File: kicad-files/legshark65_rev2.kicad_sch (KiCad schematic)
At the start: 183 parts, among them J1 ARM JTAG, J2 Conn_01x04, SW1 K2-1187SQ-A4SW-06, SW2 PCM12SMTR, T2 53261-0471, U1 STM32F411CEU6, U3 AT24C256C-SSHL-T, Y1 TAXM8M4RFDCET2T

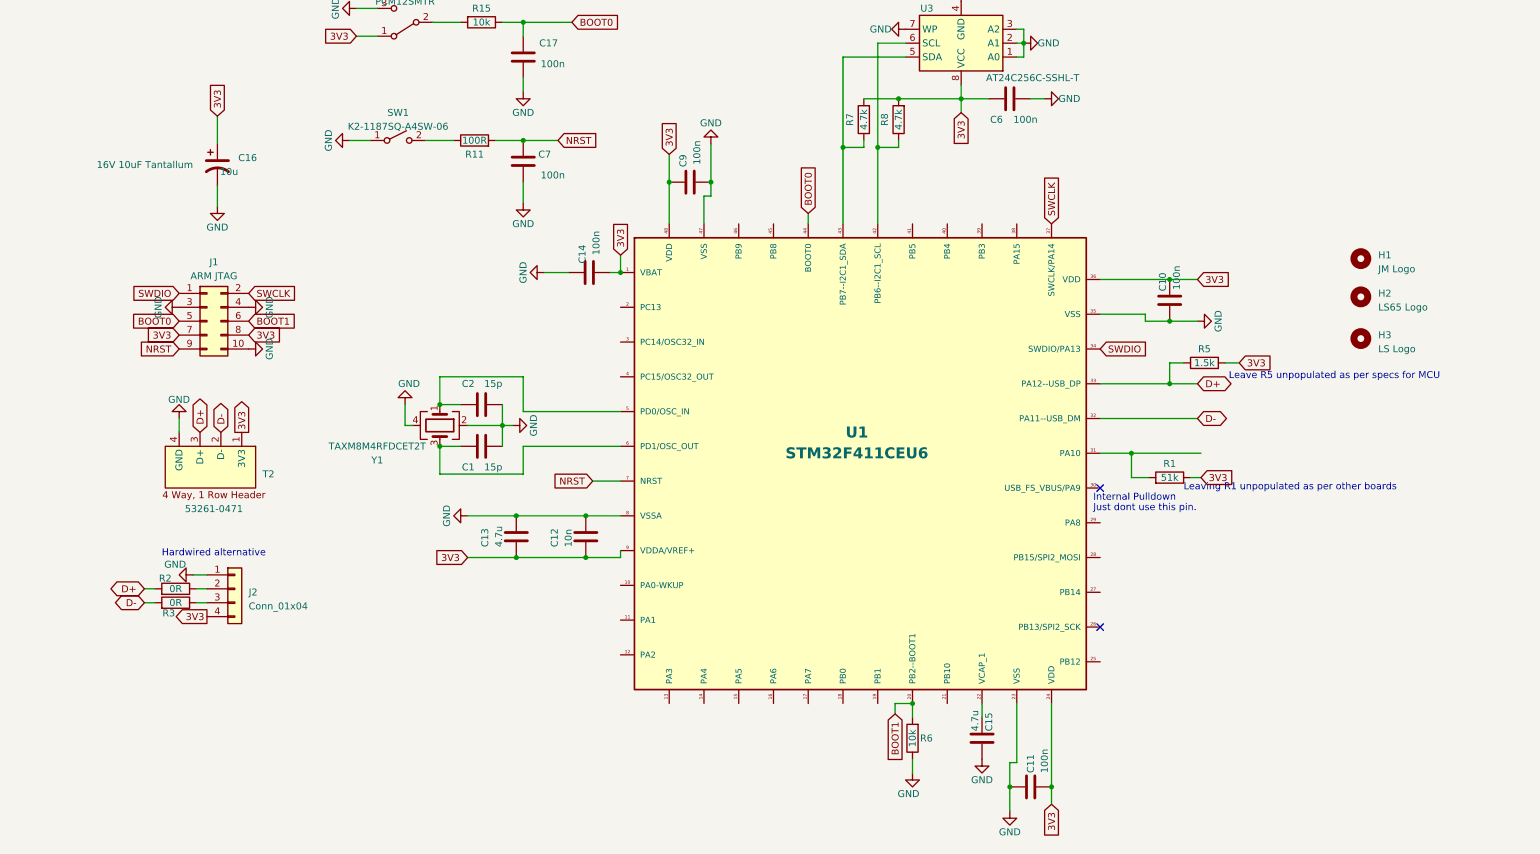
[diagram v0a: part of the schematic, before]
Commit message: Added the 5V to 3V3 stepdown schematic from db to the mb
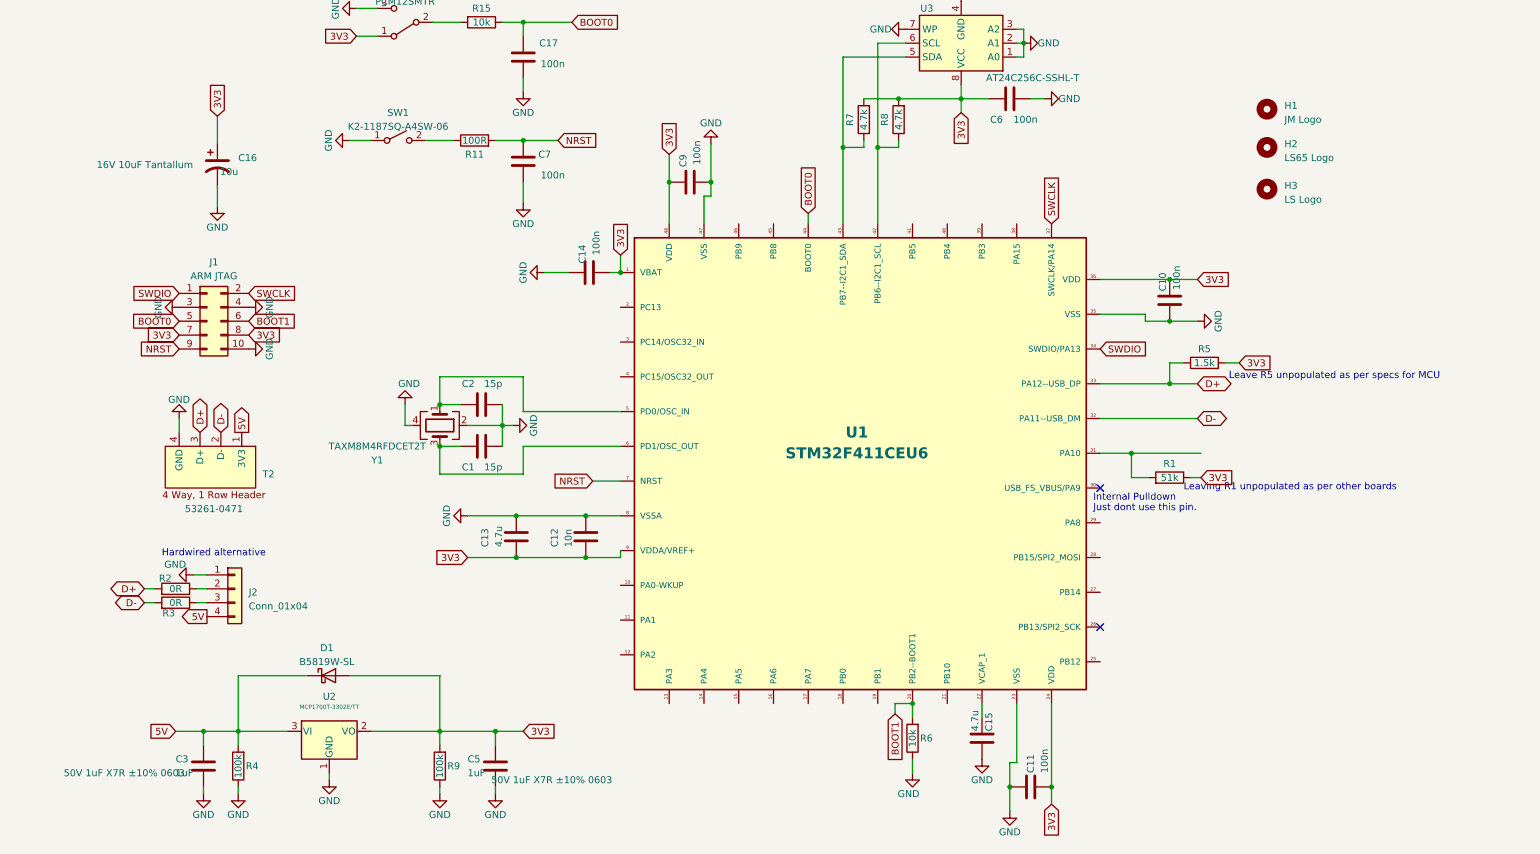
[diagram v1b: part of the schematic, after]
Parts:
- added C3, C5: 1uF, Capacitor_SMD:C_0603_1608Metric, symbol Device:C
- added D1: B5819W-SL, Diode_SMD:D_SOD-123, symbol Device:D_Schottky
- added R4, R9: 100k, Resistor_SMD:R_0402_1005Metric, symbol Device:R
- added U2: MCP1700T-3302E/TT, Package_TO_SOT_SMD:SOT-23, symbol Regulator_Linear:MCP1700-3302E_SOT23
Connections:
- net 3V3: now also C5.1, D1.2 (A), R9.2, U2.2 (VO); no longer J2.4 (Pin_4), T2.1 (3V3)
- net GND: now also C3.2, C5.2, R4.1, R9.1, U2.1 (GND)
- new net 5V: C3.1, D1.1 (K), J2.4 (Pin_4), R4.2, T2.1 (3V3), U2.3 (VI)
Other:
- moved on the sheet: H1, H2, H3

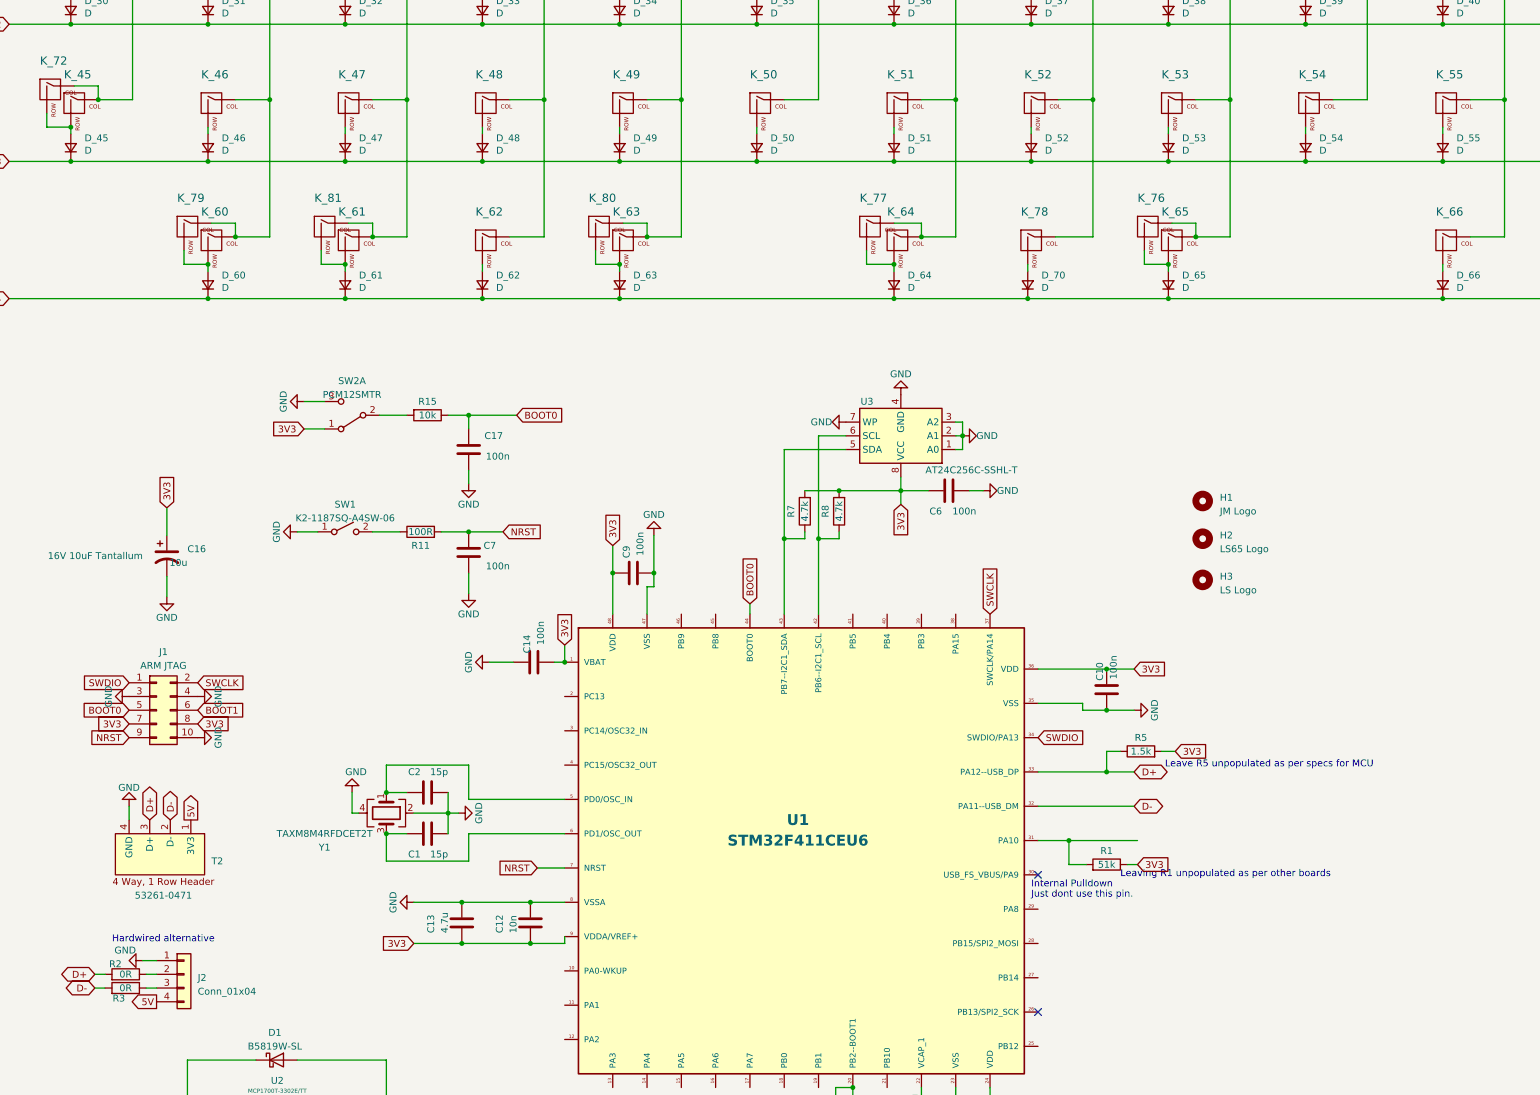
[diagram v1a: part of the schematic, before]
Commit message: Ripped up traces and started placing io
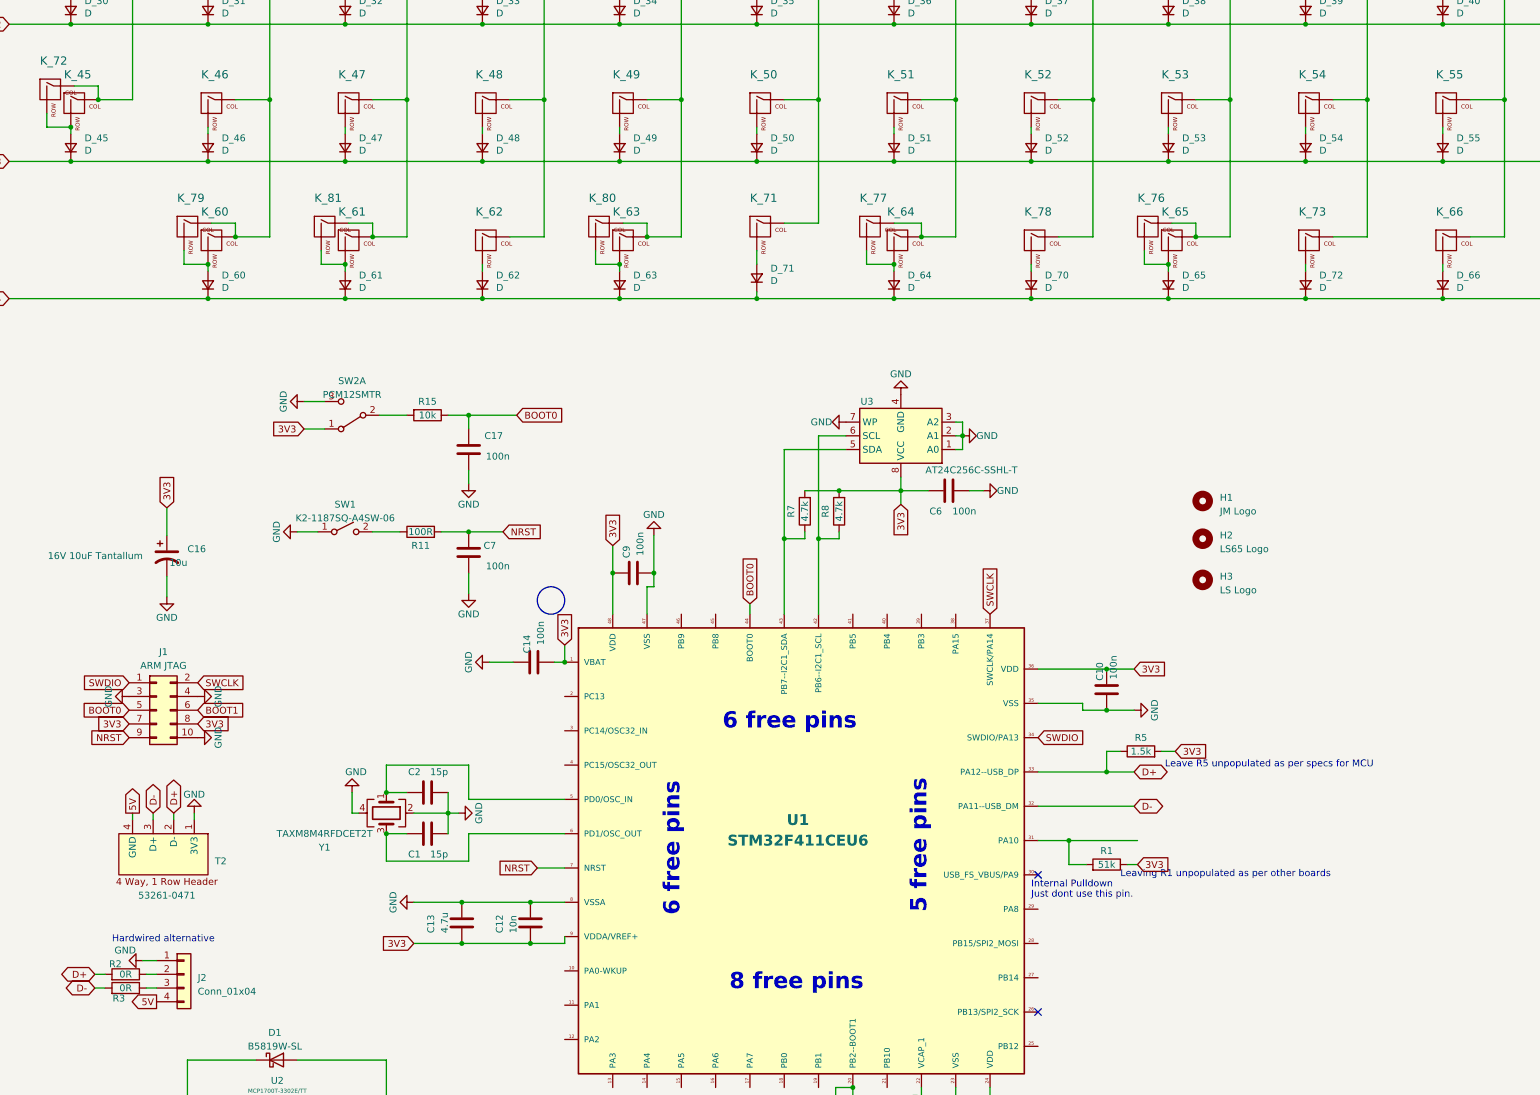
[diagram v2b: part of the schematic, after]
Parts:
- added D_71, D_72: D, Diode_SMD:D_SOD-523, symbol Device:D_Small
- added K_71, K_73: KEYSW, MX_Only:MXOnly-1U-NoLED, symbol MX_Alps_Hybrid:MX-NoLED
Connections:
- net 5V: now also T2.4 (GND); no longer T2.1 (3V3)
- net D+: now also T2.2 (D-); no longer T2.3 (D+)
- net D-: now also T2.3 (D+); no longer T2.2 (D-)
- net GND: now also T2.1 (3V3); no longer T2.4 (GND)
- net col5: now also K_71.1 (COL)
- net col9: now also K_73.1 (COL)
- net row4: now also D_71.1 (K), D_72.1 (K)
- new net: D_71.2 (A), K_71.2 (ROW)
- new net: D_72.2 (A), K_73.2 (ROW)
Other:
- note added: "5 free pins"
- note added: "6 free pins"
- note added: "8 free pins"
- moved on the sheet: D_70, K_78, T2
